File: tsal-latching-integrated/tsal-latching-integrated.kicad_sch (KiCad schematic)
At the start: 55 parts, among them J1 Conn_02x06_Counter_Clockwise, J2 Conn_02x06_Counter_Clockwise, K1 G5Q-1EU DC12, K2 G5Q-1EU DC12, Q1 XP262N7002TR-G, Q12 AO3400A, Q2 XP262N7002TR-G, Q3 XP262N7002TR-G, Q4 XP262N7002TR-G, Q5 FDN359BN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

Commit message: 11/03
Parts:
- removed H5, H6: MountingHole, MountingHole:MountingHole_3.2mm_M3, symbol Mechanical:MountingHole
- added J3: Conn_02x06_Counter_Clockwise, Connector_Molex:Molex_Micro-Fit_3.0_43045-1212_2x06_P3.00mm_Vertical, symbol Connector_Generic:Conn_02x06_Counter_Clockwise
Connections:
- net +12V: now also J3.1 (Pin_1), J3.2 (Pin_2), J3.3 (Pin_3), J3.4 (Pin_4)
- net GND: now also J3.5 (Pin_5), J3.6 (Pin_6), J3.7 (Pin_7), J3.8 (Pin_8)
- no-connect marks 3 -> 7
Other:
- note added: "Power For Other Boards"
- moved on the sheet: Q12, R23, R24

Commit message: 11/03
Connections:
- net +12A V: now also J3.1 (Pin_1), J3.2 (Pin_2), J3.3 (Pin_3), J3.4 (Pin_4)
- net +12V: no longer J3.1 (Pin_1), J3.2 (Pin_2), J3.3 (Pin_3), J3.4 (Pin_4)
- net GND: no longer J1.7 (Pin_7)
- no-connect marks 7 -> 8
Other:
- note added: "Latching Connector"
- note added: "TSAL Connector"

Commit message: Tidied up schematic and layout
TODO: Finish Layout
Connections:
- net +12A V: now also J3.5 (Pin_5), J3.6 (Pin_6)
- net +12V: now also J1.8 (Pin_8); no longer J1.12 (Pin_12)
- net GND: now also J1.7 (Pin_7), J2.4 (Pin_4), J3.10 (Pin_10), J3.11 (Pin_11), J3.12 (Pin_12), J3.9 (Pin_9); no longer J1.11 (Pin_11), J2.6 (Pin_6), J3.5 (Pin_5), J3.6 (Pin_6)
- net GREEN_LED_ON: no longer Q6.1 (G), R22.2
- net IMD_OK: now also J1.3 (Pin_3); no longer J1.1 (Pin_1)
- net SHUTDOWN_IN: now also J1.12 (Pin_12); no longer J1.10 (Pin_10)
- net SHUTDOWN_OUT: now also J1.11 (Pin_11); no longer J1.9 (Pin_9)
- net ~{BMS_DISCHG_EN}: now also J1.1 (Pin_1); no longer J1.3 (Pin_3)
- net ~{BMS_FAULT}: now also J1.9 (Pin_9); no longer J1.2 (Pin_2)
- net Reset Button GND: now reaches R10.2
- net Reset Button GND: now also J1.5 (Pin_5); no longer J1.8 (Pin_8)
- net BMS_LED_K: now reaches J1.4 (Pin_4)
- net BMS_LED_K: now also R15.2; no longer R14.2
- net at J2.5 (Pin_5), Q5.3 (D): no longer J2.3 (Pin_3)
- net RED_LED_ON renamed RED_LED_ENABLED
- net RED_LED_ENABLED: now also J2.2 (Pin_2)
- new net: J2.6 (Pin_6), Q6.3 (D)
- new net GREEN_LED_ENABLED: J2.3 (Pin_3), Q6.1 (G), R22.2
- new net IMD_LED_K: J1.2 (Pin_2), R14.2
- no-connect marks 8 -> 4
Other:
- sheet Implausibility and LED logic renamed LED logic
- sheet LED logic ports: added GREEN_LED_ENABLED, GREEN_LED_ON, RED_LED_ENABLED; removed RED_LED_ON
- moved on the sheet: J1, J3

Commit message: Updated Schematic and PCB
Rerouted Latching and changed schematic of TSAL
TODO: reroute TSAL
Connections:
- net BMS_LED_K: now also J1.3 (Pin_3); no longer J1.4 (Pin_4)
- net IMD_OK: now also J1.9 (Pin_9); no longer J1.3 (Pin_3)
- net Reset Button GND: now also J1.4 (Pin_4); no longer J1.5 (Pin_5)
- net SHUTDOWN_IN: now also J1.6 (Pin_6)
- net SHUTDOWN_OUT: now also J1.5 (Pin_5)
- net ~{BMS_FAULT}: now also J1.10 (Pin_10); no longer J1.9 (Pin_9)
- net LVS: no longer names the net of J2.9 (Pin_9)
- no-connect marks 4 -> 3
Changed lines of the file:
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@@
 	)
 	(no_connect
-		(at 29.21 64.77)
-	)
-	(no_connect
 		(at 288.925 71.12)
 	)
@@
 	)
 	(no_connect
-		(at 41.91 57.15)
+		(at 138.43 227.33)
 	)
 	(bus_entry
@@
 	(wire
 		(pts
+			(xy 153.67 262.89) (xy 161.29 262.89)
+		)
+		(stroke
+			(width 0)
+			(type default)
+		)
+	)
+	(wire
+		(pts
 			(xy 198.755 51.435) (xy 198.755 53.975)
 		)
@@
 	(wire
 		(pts
-			(xy 142.24 259.08) (xy 182.88 259.08)
-		)
-		(stroke
-			(width 0)
-			(type default)
-		)
-	)
-	(wire
-		(pts
 			(xy 226.695 267.97) (xy 232.41 267.97)
 		)
@@
 	(wire
 		(pts
-			(xy 142.24 259.08) (xy 142.24 227.33)
-		)
-		(stroke
-			(width 0)
-			(type default)
-		)
-	)
-	(wire
-		(pts
 			(xy 60.96 38.1) (xy 67.31 38.1)
 		)
@@
 		)
 	)
-	(wire
-		(pts
-			(xy 138.43 227.33) (xy 142.24 227.33)
-		)
-		(stroke
-			(width 0)
-			(type default)
-		)
-	)
 	(polyline
 		(pts
@@
 	(wire
 		(pts
+			(xy 161.29 259.08) (xy 182.88 259.08)
+		)
+		(stroke
+			(width 0)
+			(type default)
+		)
+	)
+	(wire
+		(pts
 			(xy 69.85 30.48) (xy 72.39 30.48)
 		)
@@
 		)
 	)
+	(wire
+		(pts
+			(xy 41.91 57.15) (xy 43.18 57.15)
+		)
+		(stroke
+			(width 0)
+			(type default)
+		)
+	)
 	(polyline
 		(pts
@@
 		)
 	)
+	(wire
+		(pts
+			(xy 161.29 259.08) (xy 161.29 262.89)
+		)
+		(stroke
+			(width 0)
+			(type default)
+		)
+	)
 	(polyline
 		(pts
@@
 		)
 	)
+	(label "~{BMS_FAULT}"
+		(at 43.18 57.15 0)
+		(fields_autoplaced yes)
+		(effects
+			(font
+				(size 1.27 1.27)
+			)
+			(justify left bottom)
+		)
+	)
 	(label "{LATCH_STATUS}"
 		(at 273.685 116.84 270)
@@
 		)
 	)
-	(label "Reset Button GND"
-		(at 29.21 62.23 180)
+	(label "IMD_OK"
+		(at 43.18 59.69 0)
 		(fields_autoplaced yes)
 		(effects
@@
 				(size 1.27 1.27)
 			)
-			(justify right bottom)
+			(justify left bottom)
 		)
 	)
@@
 		)
 	)
+	(label "SHUTDOWN_OUT"
+		(at 29.21 62.23 180)
+		(fields_autoplaced yes)
+		(effects
+			(font
+				(size 1.27 1.27)
+			)
+			(justify right bottom)
+		)
+	)
 	(label "BMS_FAULT_LATCHED"
 		(at 267.335 109.855 180)
@@
 		)
 	)
+	(label "SHUTDOWN_IN"
+		(at 43.18 52.07 0)
+		(fields_autoplaced yes)
+		(effects
+			(font
+				(size 1.27 1.27)
+			)
+			(justify left bottom)
+		)
+	)
 	(label "~{BMS_FAULT}"
 		(at 31.75 124.46 0)
@@
 		)
 	)
-	(label "BATT+"
-		(at 162.56 254 0)
+	(label "BMS_LED_K"
+		(at 29.21 57.15 180)
 		(fields_autoplaced yes)
 		(effects
@@
 				(size 1.27 1.27)
 			)
-			(justify left bottom)
+			(justify right bottom)
 		)
 	)
-	(label "GREEN_LED_ENABLED"
-		(at 71.12 238.76 0)
+	(label "BATT+"
+		(at 162.56 254 0)
 		(fields_autoplaced yes)
 		(effects
@@
 		)
 	)
-	(label "BMS_LED_K"
-		(at 29.21 59.69 180)
+	(label "GREEN_LED_ENABLED"
+		(at 71.12 238.76 0)
 		(fields_autoplaced yes)
 		(effects
@@
 				(size 1.27 1.27)
 			)
-			(justify right bottom)
+			(justify left bottom)
 		)
 	)
@@
 		)
 	)
+	(label "Reset Button GND"
+		(at 29.21 59.69 180)
+		(fields_autoplaced yes)
+		(effects
+			(font
+				(size 1.27 1.27)
+			)
+			(justify right bottom)
+		)
+	)
 	(label "GREEN_LED_ON"
 		(at 257.81 220.98 0)
@@
 		)
 	)
-	(label "DCLINK_HV_DETECTED"
-		(at 203.2 219.71 0)
+	(label "IMD_LED_K"
+		(at 29.21 54.61 180)
 		(fields_autoplaced yes)
 		(effects
@@
 				(size 1.27 1.27)
 			)
-			(justify left bottom)
+			(justify right bottom)
 		)
 	)
-	(label "IMD_FAULT_LATCHED"
-		(at 347.98 127 270)
+	(label "DCLINK_HV_DETECTED"
+		(at 203.2 219.71 0)
 		(fields_autoplaced yes)
 		(effects
@@
 				(size 1.27 1.27)
 			)
-			(justify right bottom)
+			(justify left bottom)
 		)
 	)
-	(label "IMD_LED_K"
-		(at 29.21 54.61 180)
+	(label "IMD_FAULT_LATCHED"
+		(at 347.98 127 270)
 		(fields_autoplaced yes)
 		(effects
@@
 		)
 	)
+	(label "SHUTDOWN_IN"
+		(at 29.21 64.77 180)
+		(fields_autoplaced yes)
+		(effects
+			(font
+				(size 1.27 1.27)
+			)
+			(justify right bottom)
+		)
+	)
 	(label "LVS"
 		(at 162.56 259.08 0)
@@
 		)
 	)
-	(label "IMD_OK"
-		(at 29.21 57.15 180)
-		(fields_autoplaced yes)
-		(effects
-			(font
-				(size 1.27 1.27)
-			)
-			(justify right bottom)
-		)
-	)
 	(label "GREEN_LED_ENABLED"
 		(at 354.33 224.79 180)
@@
 		)
 	)
-	(label "~{BMS_FAULT}"
-		(at 43.18 59.69 0)
-		(fields_autoplaced yes)
-		(effects
-			(font
-				(size 1.27 1.27)
-			)
-			(justify left bottom)
-		)
-	)
-	(label "SHUTDOWN_IN"
-		(at 58.42 52.07 180)
-		(fields_autoplaced yes)
-		(effects
-			(font
-				(size 1.27 1.27)
-			)
-			(justify right bottom)
-		)
-	)
 	(label "SHUTDOWN_IN"
 		(at 283.845 46.355 270)
@@
 					(unit 1)
 				)
+			)
+		)
+	)
+	(symbol
+		(lib_id "power:+12V")
+		(at 153.67 262.89 0)
+		(unit 1)
+		(exclude_from_sim no)
+		(in_bom yes)
+		(on_board yes)
+		(dnp no)
+		(property "Reference" "#PWR021"
+			(at 153.67 266.7 0)
+			(effects
+				(font
+					(size 1.27 1.27)
+				)
+				(hide yes)
+			)
+		)
+		(property "Value" "+12A V"
+			(at 153.67 259.08 0)
+			(effects
+				(font
+					(size 1.27 1.27)
+				)
+			)
+		)
+		(property "Footprint" ""
+			(at 153.67 262.89 0)
+			(effects
+				(font
+					(size 1.27 1.27)
+				)
+				(hide yes)
+			)
+		)
+		(property "Datasheet" ""
+			(at 153.67 262.89 0)
+			(effects
+				(font
+					(size 1.27 1.27)
+				)
+				(hide yes)
+			)
+		)
+		(property "Description" ""
+			(at 153.67 262.89 0)
+			(effects
+				(font
+					(size 1.27 1.27)
+				)
+				(hide yes)
+			)
+		)
+		(pin "1"
+		)
+		(instances
+			(project "tsal-latching-integrated"
+				(path "/50f6117a-e039-4744-a8aa-10bac8a7c3af"
+					(reference "#PWR021")
+					(unit 1)
+				)

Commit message: Rewired TSAL and updated silkscreen
TODO: Change relays to solid state
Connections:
- net +12A V: no longer J2.1 (Pin_1), J3.1 (Pin_1), J3.2 (Pin_2), J3.3 (Pin_3), J3.4 (Pin_4), J3.5 (Pin_5), J3.6 (Pin_6)
- net BATT+: now also J2.12 (Pin_12); no longer J2.11 (Pin_11)
- net GND: now also J2.2 (Pin_2), J2.6 (Pin_6); no longer J2.10 (Pin_10), J2.4 (Pin_4)
- net GREEN_LED_ENABLED: now also J2.4 (Pin_4); no longer J2.3 (Pin_3)
- net GREEN_LED_ON: now also J2.5 (Pin_5)
- net RED_LED_ENABLED: now also J2.11 (Pin_11); no longer J2.2 (Pin_2)
- net GREEN.LED.K: now reaches Q6.3 (D)
- net GREEN.LED.K: now also J2.3 (Pin_3); no longer J2.6 (Pin_6)
- net TS.DETECTED: now reaches R18.2, R21.2
- net TS.DETECTED: now also J2.9 (Pin_9); no longer J2.12 (Pin_12)
- net RED.LED.K: now reaches Q5.3 (D)
- net RED.LED.K: now also J2.10 (Pin_10); no longer J2.5 (Pin_5)
- net Power Latch/LATCH_RESET+ renamed LATCH.RESET+
- net Power Latch/LATCH_RESET- renamed LATCH.RESET-
- new net +12AO V: J2.1 (Pin_1), J3.1 (Pin_1), J3.2 (Pin_2), J3.3 (Pin_3), J3.4 (Pin_4), J3.5 (Pin_5), J3.6 (Pin_6)
- no-connect marks 3 -> 2
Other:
- moved on the sheet: H1, H2, H3, H4, J2, Q5, Q6, R22, R38

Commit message: Added SS relay, moved power connector
Ready for design review
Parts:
- removed D4, D7: BAT54W, Package_TO_SOT_SMD:SOT-323_SC-70, symbol Diode:BAT54W
- added Q13, Q14, Q15, Q16: SiS413DNT, Package_SO:Vishay_PowerPAK_1212-8_Single, symbol SUFST:SiS413DNT
- added R25, R28, R30, R32: 0, Resistor_SMD:R_0805_2012Metric_Pad1.20x1.40mm_HandSolder, symbol Device:R
- added R26, R27, R29, R31: 10k, Resistor_SMD:R_0805_2012Metric_Pad1.20x1.40mm_HandSolder, symbol Device:R
- H1, H2, H3, H4: value MountingHole -> M3
- J1, J2, J3: footprint Connector_Molex:Molex_Micro-Fit_3.0_43045-1212_2x06_P3.00mm_Vertical -> Connector_Molex:Molex_Micro-Fit_3.0_43045-1200_2x06_P3.00mm_Horizontal
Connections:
- net +12AO V: no longer J3.6 (Pin_6)
- net +12V: now also J3.6 (Pin_6), R25.1, R30.1; no longer J1.8 (Pin_8)
- net BMS_LED_K: now also J1.2 (Pin_2); no longer J1.3 (Pin_3)
- net GND: now also J1.10 (Pin_10); no longer J1.7 (Pin_7)
- net GREEN_LED_ON: now also J2.11 (Pin_11); no longer J2.5 (Pin_5)
- net IMD_LED_K: now also J1.1 (Pin_1); no longer J1.2 (Pin_2)
- net IMD_OK: now also J1.8 (Pin_8); no longer J1.9 (Pin_9)
- net RED_LED_ENABLED: now also J2.5 (Pin_5); no longer J2.11 (Pin_11)
- net SHUTDOWN_IN: now also Q13.1 (S), Q13.2 (S), Q13.3 (S), R26.1
- net SHUTDOWN_OUT: now also Q16.5 (D)
- net ~{BMS_DISCHG_EN}: now also J1.7 (Pin_7); no longer J1.1 (Pin_1)
- net ~{BMS_FAULT}: now also J1.9 (Pin_9); no longer J1.10 (Pin_10)
- net at K1.1, Q1.3 (D): now also R28.2
- net at K2.1, Q3.3 (D): now also R32.2
- net at K1.2, K2.3: now also Q14.5 (D), Q15.1 (S), Q15.2 (S), Q15.3 (S), R29.1
- net Reset Button GND renamed Reset Button +
- new net: Q15.4 (G), Q16.4 (G), R29.2, R30.2, R31.2, R32.1
- new net: Q13.4 (G), Q14.4 (G), R25.2, R26.2, R27.2, R28.1
- new net: Q13.5 (D), Q14.1 (S), Q14.2 (S), Q14.3 (S), R27.1
- new net: Q15.5 (D), Q16.1 (S), Q16.2 (S), Q16.3 (S), R31.1
- no-connect marks 2 -> 3
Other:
- note added: "Power"
- note removed: "Power For Other Boards"
- moved on the sheet: C1, C7, C8, Q1, Q3, R1, R2, R21, R38, R7, R8, R9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

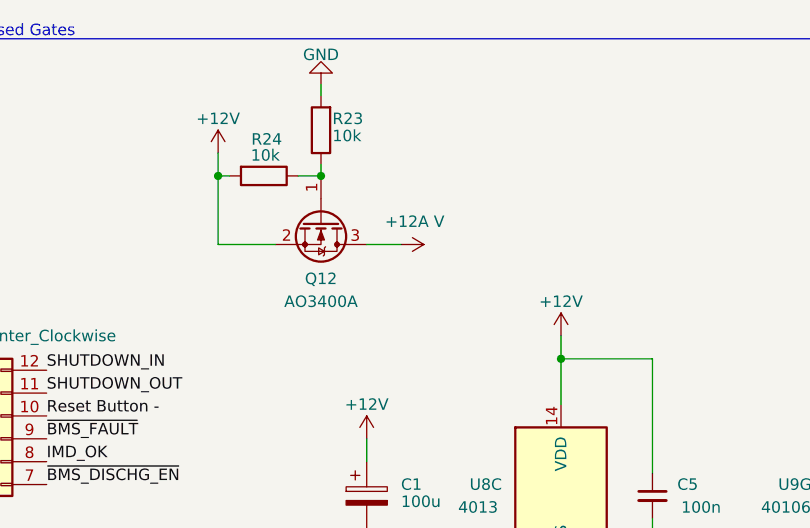
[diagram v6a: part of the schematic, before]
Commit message: fixed ERC error
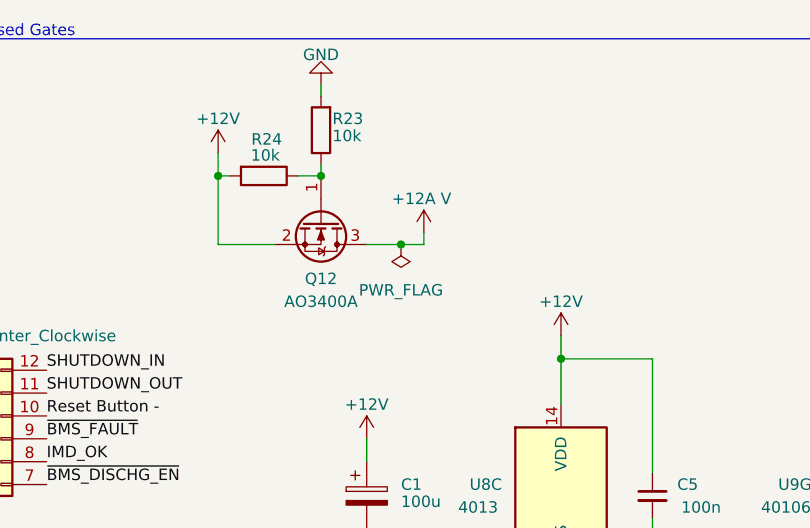
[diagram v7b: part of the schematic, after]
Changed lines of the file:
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@@
 	)
 	(junction
+		(at 81.28 38.1)
+		(diameter 0)
+		(color 0 0 0 0)
+	)
+	(junction
 		(at 133.35 81.28)
 		(diameter 0)
@@
 	(wire
 		(pts
+			(xy 83.82 38.1) (xy 81.28 38.1)
+		)
+		(stroke
+			(width 0)
+			(type default)
+		)
+	)
+	(wire
+		(pts
 			(xy 309.88 78.105) (xy 309.88 86.36)
 		)
@@
 	(wire
 		(pts
+			(xy 77.47 38.1) (xy 81.28 38.1)
+		)
+		(stroke
+			(width 0)
+			(type default)
+		)
+	)
+	(wire
+		(pts
 			(xy 284.48 66.04) (xy 288.925 66.04)
 		)
@@
 	(wire
 		(pts
+			(xy 83.82 36.83) (xy 83.82 38.1)
+		)
+		(stroke
+			(width 0)
+			(type default)
+		)
+	)
+	(wire
+		(pts
 			(xy 109.22 50.8) (xy 109.22 63.5)
 		)
@@
 	(wire
 		(pts
-			(xy 81.28 38.1) (xy 77.47 38.1)
-		)
-		(stroke
-			(width 0)
-			(type default)
-		)
-	)
-	(wire
-		(pts
 			(xy 288.925 66.04) (xy 290.83 66.04)
 		)
@@
 	)
 	(symbol
+		(lib_id "power:PWR_FLAG")
+		(at 81.28 38.1 180)
+		(unit 1)
+		(exclude_from_sim no)
+		(in_bom yes)
+		(on_board yes)
+		(dnp no)
+		(fields_autoplaced yes)
+		(property "Reference" "#FLG02"
+			(at 81.28 40.005 0)
+			(effects
+				(font
+					(size 1.27 1.27)
+				)
+				(hide yes)
+			)
+		)
+		(property "Value" "PWR_FLAG"
+			(at 81.28 43.18 0)
+			(effects
+				(font
+					(size 1.27 1.27)
+				)
+			)
+		)
+		(property "Footprint" ""
+			(at 81.28 38.1 0)
+			(effects
+				(font
+					(size 1.27 1.27)
+				)
+				(hide yes)
+			)
+		)
+		(property "Datasheet" "~"
+			(at 81.28 38.1 0)
+			(effects
+				(font
+					(size 1.27 1.27)
+				)
+				(hide yes)
+			)
+		)
+		(property "Description" ""
+			(at 81.28 38.1 0)
+			(effects
+				(font
+					(size 1.27 1.27)
+				)
+				(hide yes)
+			)
+		)
+		(pin "1"
+		)
+		(instances
+			(project "tsal-latching-integrated"
+				(path "/50f6117a-e039-4744-a8aa-10bac8a7c3af"
+					(reference "#FLG02")
+					(unit 1)
+				)
+			)
+		)
+	)
+	(symbol
 		(lib_id "Device:R")
 		(at 313.69 86.36 90)
@@
 	(symbol
 		(lib_id "power:+12V")
-		(at 81.28 38.1 270)
+		(at 83.82 36.83 0)
 		(unit 1)
 		(exclude_from_sim no)
@@
 		(dnp no)
 		(property "Reference" "#PWR036"
-			(at 77.47 38.1 0)
+			(at 83.82 40.64 0)
 			(effects
 				(font
@@
 		)
 		(property "Value" "+12A V"
-			(at 82.804 35.56 90)
+			(at 83.566 33.02 0)
 			(effects
 				(font
@@
 		)
 		(property "Footprint" ""
-			(at 81.28 38.1 0)
+			(at 83.82 36.83 0)
 			(effects
 				(font
@@
 		)
 		(property "Datasheet" ""
-			(at 81.28 38.1 0)
+			(at 83.82 36.83 0)
 			(effects
 				(font
@@
 		)
 		(property "Description" ""
-			(at 81.28 38.1 0)
+			(at 83.82 36.83 0)
 			(effects
 				(font

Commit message: misc small fixes
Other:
- moved on the sheet: R26, R27, R29, R31
